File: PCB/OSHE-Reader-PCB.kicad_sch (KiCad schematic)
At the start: 11 parts

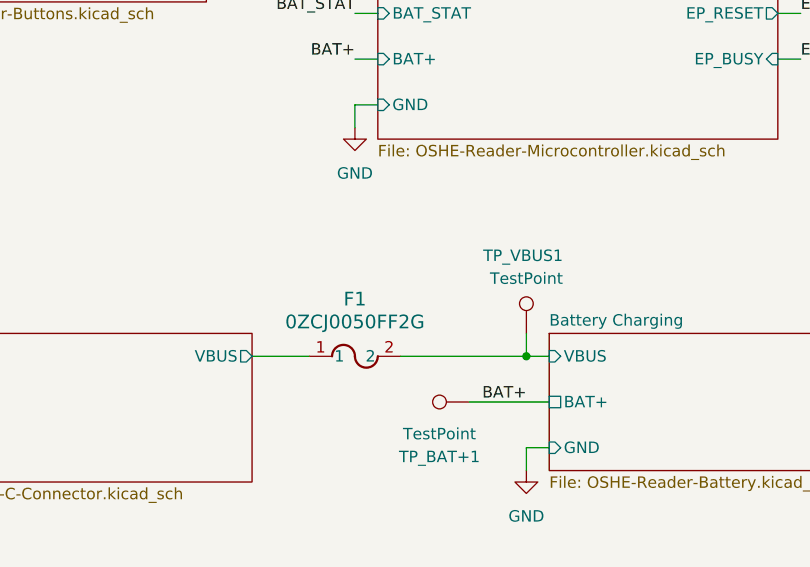
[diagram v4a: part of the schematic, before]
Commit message: PCB and Schematic update
added the Schottky diode to PCB and Schematic
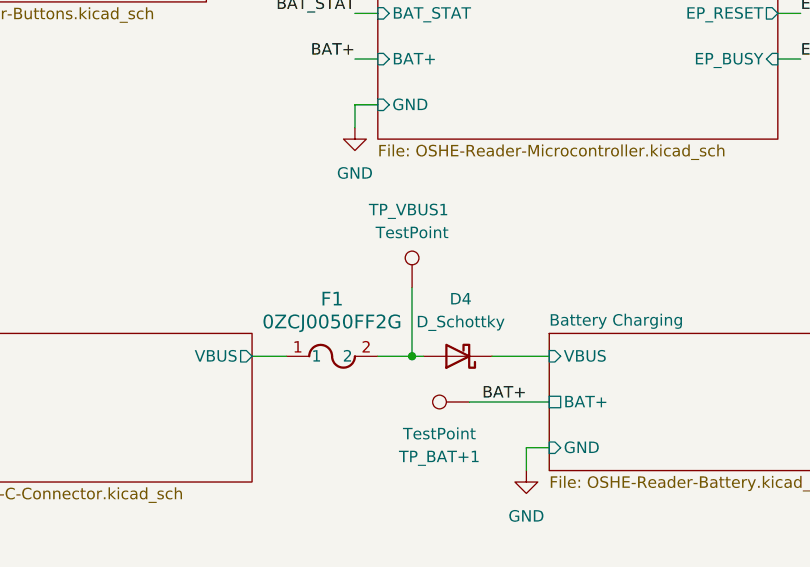
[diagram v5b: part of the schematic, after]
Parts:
- added D4: D_Schottky, Diode_SMD:D_1206_3216Metric_Pad1.42x1.75mm_HandSolder, symbol Device:D_Schottky
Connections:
- net Battery Charging/VBUS: now also D4.1 (K); no longer F1.2, TP_VBUS1.1
- new net: D4.2 (A), F1.2, TP_VBUS1.1
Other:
- moved on the sheet: F1, TP_VBUS1
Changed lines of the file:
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@@
-	)
-	(junction
-		(at 114.3 129.54)
-		(diameter 0)
-		(color 0 0 0 0)
 	)
 	(junction
@@
 	)
 	(junction
+		(at 101.6 129.54)
+		(diameter 0)
+		(color 0 0 0 0)
+	)
+	(junction
 		(at 33.02 140.97)
 		(diameter 0)
@@
 	(wire
 		(pts
+			(xy 101.6 129.54) (xy 102.87 129.54)
+		)
+		(stroke
+			(width 0)
+			(type default)
+		)
+	)
+	(wire
+		(pts
 			(xy 210.82 93.98) (xy 213.36 93.98)
 		)
@@
 	(wire
 		(pts
-			(xy 100.33 129.54) (xy 114.3 129.54)
-		)
-		(stroke
-			(width 0)
-			(type default)
-		)
-	)
-	(wire
-		(pts
 			(xy 38.1 86.36) (xy 40.64 86.36)
 		)
@@
 	(wire
 		(pts
-			(xy 114.3 129.54) (xy 116.84 129.54)
+			(xy 110.49 129.54) (xy 116.84 129.54)
 		)
 		(stroke
@@
 	(wire
 		(pts
-			(xy 83.82 129.54) (xy 90.17 129.54)
+			(xy 83.82 129.54) (xy 87.63 129.54)
 		)
 		(stroke
@@
 	(wire
 		(pts
+			(xy 101.6 121.92) (xy 101.6 129.54)
+		)
+		(stroke
+			(width 0)
+			(type default)
+		)
+	)
+	(wire
+		(pts
 			(xy 142.24 86.36) (xy 144.78 86.36)
 		)
@@
 	(wire
 		(pts
-			(xy 114.3 127) (xy 114.3 129.54)
-		)
-		(stroke
-			(width 0)
-			(type default)
-		)
-	)
-	(wire
-		(pts
 			(xy 162.56 93.98) (xy 160.02 93.98)
 		)
@@
 		(pts
 			(xy 142.24 91.44) (xy 144.78 91.44)
+		)
+		(stroke
+			(width 0)
+			(type default)
+		)
+	)
+	(wire
+		(pts
+			(xy 97.79 129.54) (xy 101.6 129.54)
 		)
 		(stroke
@@
 	(symbol
 		(lib_id "0ZCJ0050FF2G:0ZCJ0050FF2G")
-		(at 90.17 129.54 0)
+		(at 87.63 129.54 0)
 		(unit 1)
 		(exclude_from_sim no)
@@
 		(fields_autoplaced yes)
 		(property "Reference" "F1"
-			(at 95.25 123.19 0)
+			(at 92.71 123.19 0)
 			(effects
 				(font
@@
 		)
 		(property "Value" "0ZCJ0050FF2G"
-			(at 95.25 125.73 0)
+			(at 92.71 125.73 0)
 			(effects
 				(font
@@
 		)
 		(property "Footprint" "0ZCJ0050FF2G:0ZCJ_BEL"
-			(at 90.17 129.54 0)
+			(at 87.63 129.54 0)
 			(effects
 				(font
@@
 		)
 		(property "Datasheet" "0ZCJ0050FF2G"
-			(at 90.17 129.54 0)
+			(at 87.63 129.54 0)
 			(effects
 				(font
@@
 		)
 		(property "Description" ""
-			(at 90.17 129.54 0)
+			(at 87.63 129.54 0)
 			(effects
 				(font
@@
 	)
 	(symbol
+		(lib_id "Device:D_Schottky")
+		(at 106.68 129.54 180)
+		(unit 1)
+		(exclude_from_sim no)
+		(in_bom yes)
+		(on_board yes)
+		(dnp no)
+		(fields_autoplaced yes)
+		(property "Reference" "D4"
+			(at 106.9975 123.19 0)
+			(effects
+				(font
+					(size 1.27 1.27)
+				)
+			)
+		)
+		(property "Value" "D_Schottky"
+			(at 106.9975 125.73 0)
+			(effects
+				(font
+					(size 1.27 1.27)
+				)
+			)
+		)
+		(property "Footprint" "Diode_SMD:D_1206_3216Metric_Pad1.42x1.75mm_HandSolder"
+			(at 106.68 129.54 0)
+			(effects
+				(font
+					(size 1.27 1.27)
+				)
+				(hide yes)
+			)
+		)
+		(property "Datasheet" "~"
+			(at 106.68 129.54 0)
+			(effects
+				(font
+					(size 1.27 1.27)
+				)
+				(hide yes)
+			)
+		)
+		(property "Description" "Schottky diode"
+			(at 106.68 129.54 0)
+			(effects
+				(font
+					(size 1.27 1.27)
+				)
+				(hide yes)
+			)
+		)
+		(pin "2"
+		)
+		(pin "1"
+		)
+		(instances
+			(project ""
+				(path "/3f072c92-e35a-4654-839b-728bd3dc3a46"
+					(reference "D4")
+					(unit 1)
+				)
+			)
+		)
+	)
+	(symbol
 		(lib_id "power:+3V3")
 		(at 38.1 63.5 0)
@@
 	(symbol
 		(lib_id "Connector:TestPoint")
-		(at 114.3 127 0)
+		(at 101.6 121.92 0)
 		(mirror y)
 		(unit 1)
@@
 		(dnp no)
 		(property "Reference" "TP_VBUS1"
-			(at 118.364 118.3639 0)
+			(at 105.664 113.2839 0)
 			(effects
 				(font
@@
 		)
 		(property "Value" "TestPoint"
-			(at 118.364 120.9039 0)
+			(at 105.664 115.8239 0)
 			(effects
 				(font
@@
 		)
 		(property "Footprint" "TestPoint:TestPoint_Keystone_5019_Miniature"
-			(at 109.22 127 0)
+			(at 96.52 121.92 0)
 			(effects
 				(font
@@
 		)
 		(property "Datasheet" "~"
-			(at 109.22 127 0)
+			(at 96.52 121.92 0)
 			(effects
 				(font
@@
 		)
 		(property "Description" "test point"
-			(at 114.3 127 0)
-			(effects
-				(font
+			(at 101.6 121.92 0)
+			(effects
+				(font

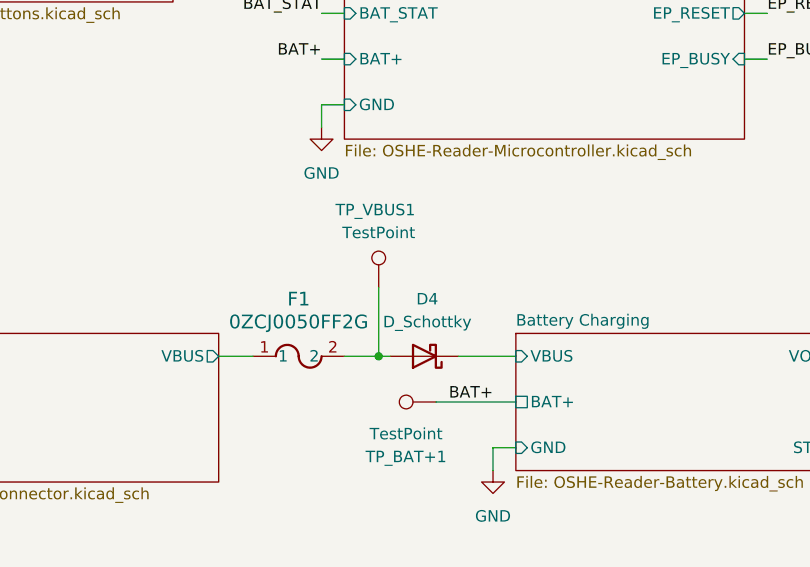
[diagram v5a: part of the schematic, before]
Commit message: Minor fixes to PCB: schottky diode for battery charging and general battery charging routing fixes
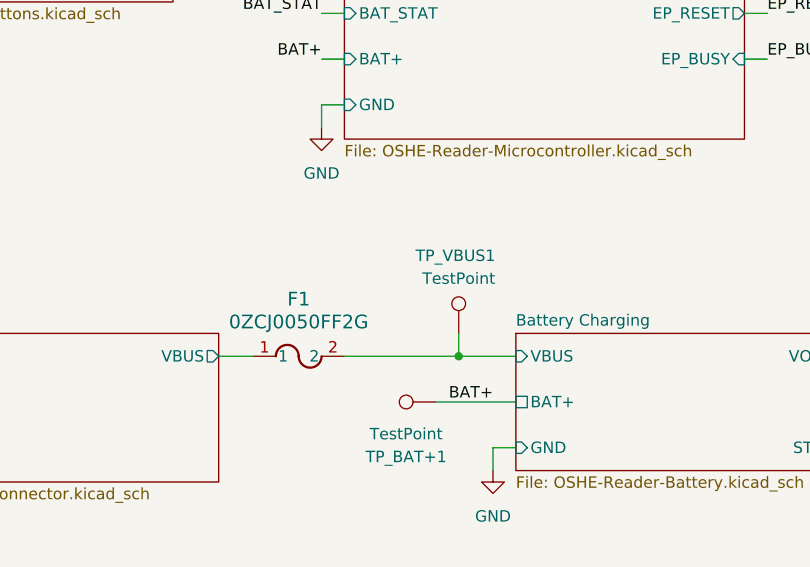
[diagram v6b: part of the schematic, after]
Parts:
- removed D4: D_Schottky, Diode_SMD:D_1206_3216Metric_Pad1.42x1.75mm_HandSolder, symbol Device:D_Schottky
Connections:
- net Battery Charging/VBUS: now also F1.2, TP_VBUS1.1
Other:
- moved on the sheet: TP_VBUS1
